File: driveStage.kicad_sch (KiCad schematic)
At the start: 67 parts, among them J1 MOD_IN, K1 DIP12-1C90-51L, Q1 SQJA70EP-T1, Q7 BSS138, SW1 SW_DIP_x03, U1 LTC6655BHLS8-4.096, U2 MAX5719xSD, U23 TL082, U3 ADA4898-1YRDZ, U4 ADA4898-1YRDZ, U6 ADA4898-1YRDZ

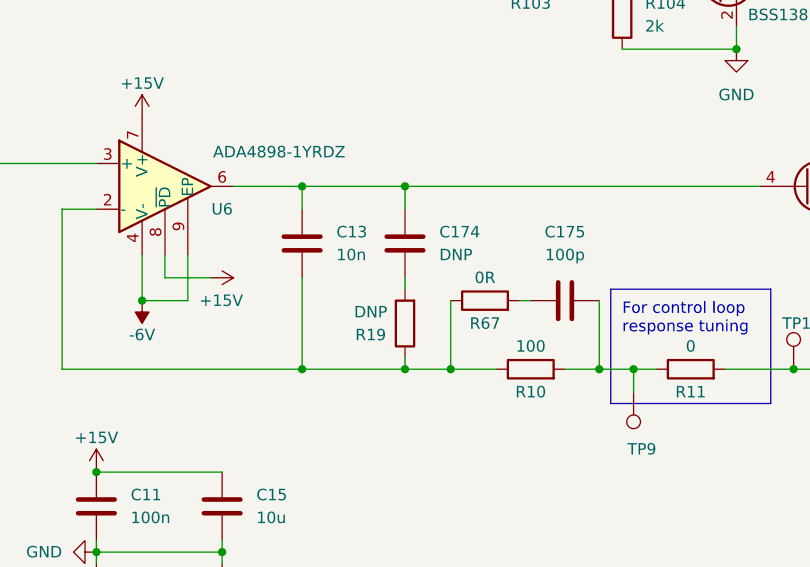
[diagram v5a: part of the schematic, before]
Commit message: sch: Set DNP for DNP components
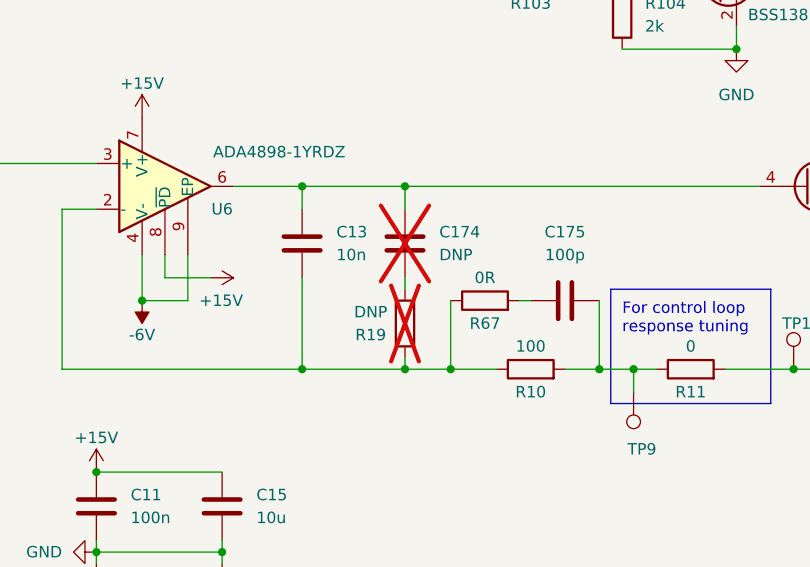
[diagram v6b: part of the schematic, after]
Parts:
- C174, R19: now not fitted
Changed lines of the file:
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@@
   )
   (symbol (lib_id "Device:R") (at 299.72 110.49 180) (unit 1)
-    (in_bom yes) (on_board yes) (dnp no)
+    (in_bom yes) (on_board yes) (dnp yes)
     (property "Reference" "R19" (at 295.91 111.76 0)
       (effects (font (size 1.27 1.27)))
@@
   )
   (symbol (lib_id "Device:C") (at 299.72 101.6 0) (unit 1)
-    (in_bom yes) (on_board yes) (dnp no) (fields_autoplaced)
+    (in_bom yes) (on_board yes) (dnp yes) (fields_autoplaced)
     (property "Reference" "C174" (at 303.53 100.3299 0)
       (effects (font (size 1.27 1.27)) (justify left))

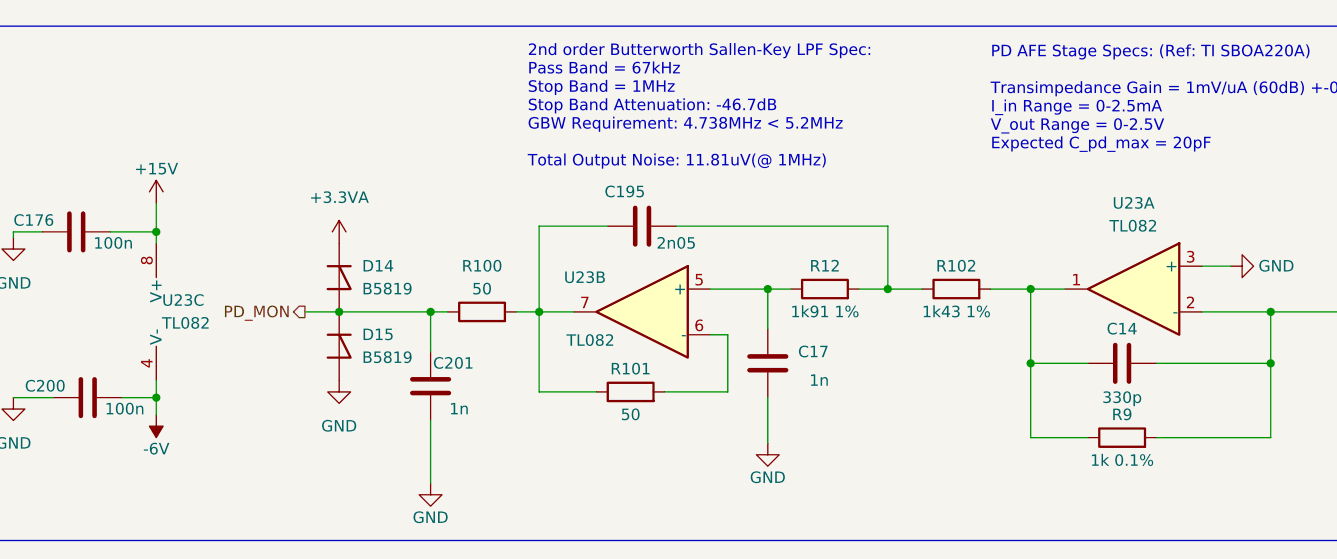
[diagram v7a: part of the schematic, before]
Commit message: footprint: Add TL082Hx TI SOIC-8 footprint
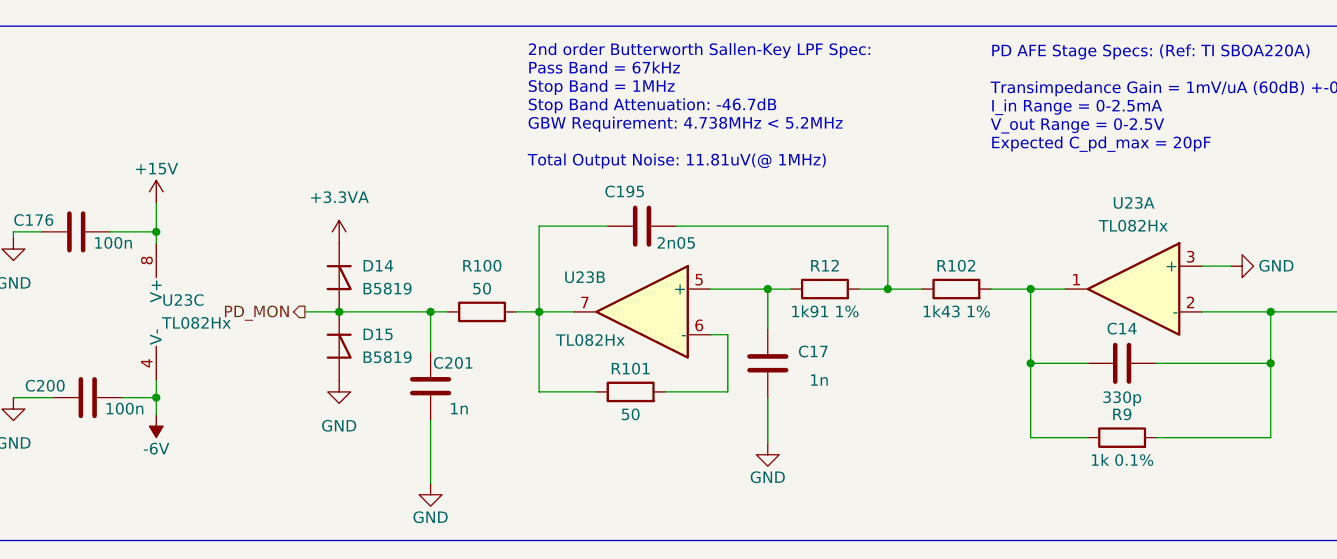
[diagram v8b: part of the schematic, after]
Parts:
- U23: value TL082 -> TL082Hx; footprint (none) -> kirdy:SOIC8-TL082Hx; MFR_PN (none) -> TL082HIDR
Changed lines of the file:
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@@
       (effects (font (size 1.27 1.27)))
     )
-    (property "Value" "TL082" (at 318.77 200.66 0)
-      (effects (font (size 1.27 1.27)))
-    )
-    (property "Footprint" "" (at 318.77 207.645 0)
+    (property "Value" "TL082Hx" (at 318.77 200.66 0)
+      (effects (font (size 1.27 1.27)))
+    )
+    (property "Footprint" "kirdy:SOIC8-TL082Hx" (at 318.77 207.645 0)
       (effects (font (size 1.27 1.27)) hide)
     )
     (property "Datasheet" "http://www.ti.com/lit/ds/symlink/tl081.pdf" (at 318.77 207.645 0)
+      (effects (font (size 1.27 1.27)) hide)
+    )
+    (property "MFR_PN" "TL082HIDR" (at 318.77 207.645 0)
       (effects (font (size 1.27 1.27)) hide)
     )
@@
       (effects (font (size 1.27 1.27)))
     )
-    (property "Value" "TL082" (at 258.445 213.36 0)
-      (effects (font (size 1.27 1.27)))
-    )
-    (property "Footprint" "" (at 264.16 210.185 0)
+    (property "Value" "TL082Hx" (at 258.445 213.36 0)
+      (effects (font (size 1.27 1.27)))
+    )
+    (property "Footprint" "kirdy:SOIC8-TL082Hx" (at 264.16 210.185 0)
       (effects (font (size 1.27 1.27)) hide)
     )
     (property "Datasheet" "http://www.ti.com/lit/ds/symlink/tl081.pdf" (at 264.16 210.185 0)
+      (effects (font (size 1.27 1.27)) hide)
+    )
+    (property "MFR_PN" "TL082HIDR" (at 264.16 210.185 0)
       (effects (font (size 1.27 1.27)) hide)
     )
@@
       (effects (font (size 1.27 1.27)) (justify right))
     )
-    (property "Value" "TL082" (at 210.82 211.455 0)
+    (property "Value" "TL082Hx" (at 210.82 211.455 0)
       (effects (font (size 1.27 1.27)) (justify right))
     )
-    (property "Footprint" "" (at 207.645 210.185 0)
+    (property "Footprint" "kirdy:SOIC8-TL082Hx" (at 207.645 210.185 0)
       (effects (font (size 1.27 1.27)) hide)
     )
@@
       (effects (font (size 1.27 1.27)) hide)
     )
+    (property "MFR_PN" "TL082HIDR" (at 207.645 210.185 0)
+      (effects (font (size 1.27 1.27)) hide)
+    )
